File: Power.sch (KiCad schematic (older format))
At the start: 46 parts, among them J7 AUX, J8 MCU_CURRENT, J9 RAM_CURRENT, Q2 IRLML6402, U1 ATXMEGA128A1U-AU, U2 SN74AHC573PW, U4 LM3671MF

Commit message: Finished?
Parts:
- removed C33, C?: 100n, IPC7351-Nominal:CAPC1005X55, symbol C-0402
- removed D?: SS12, IPC7351-Nominal:DIOM5326X292, symbol SS12
- removed Q2, Q?: IRLML6402, smd-semi:SOT-23, symbol IRLML6402
- removed Q?: MMUN2231L, smd-semi:SOT-23, symbol MMUN2231L
- removed Q?: MMUN2111L, smd-semi:SOT-23, symbol MMUN2111L
- removed R13: 100k, IPC7351-Nominal:RESCAXE80P160X320X70-8, symbol RESPACK-4X0603-CONV
- removed R? (x4): 3k3, IPC7351-Nominal:RESCAXE80P160X320X70-8, symbol RESPACK-4X0603-CONV
- added J10: POWER, conn-fci:CONN-10118194-0001LF-FCI, symbol CONN-10118194-0001LF-UUSB-B
- added R13, R16: 365, IPC7351-Nominal:RESC1005X40, symbol R-0402
- added R17: 3k3, IPC7351-Nominal:RESCAXE80P160X320X70-8, symbol RESPACK-4X0603-CONV
- added TP1: GND, manuf:TESTPOINT-KEYSTONE-5018, symbol TESTPOINT
- added U7: TPS2110A, IPC7351-Nominal:SOP65P640X110-8, symbol TPS2110A
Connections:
- net FILT_VBUS: now also U7.6 (IN2); no longer C32.1
- net GND: now also C32.1, J10.5 (GND), J10.SH (SHIELD), R13.2, R17.4, TP1.1, U7.2 (D1), U7.5 (GND)
- net VBUS: now also U7.7 (OUT)
- net ALT_VBUS: now reaches C32.2
- net ALT_VBUS: now also J10.1 (V+), R16.1, U7.8 (IN1)
- new net: R16.2, R17.1
- new net: R17.7, R17.8
- new net: R17.2, R17.3
- new net: R17.5, R17.6, U7.3 (VSNS)
- new net: R13.1, U7.4 (ILIM)
- no-connect marks 0 -> 4
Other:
- note added: "I_lim = 250V/R_lim = 685mA\nTypical inrush 250mA\nout = (in1 ≥ 3.38V ? in1 : max(in1, in2))"
- moved on the sheet: C13, C20, C21, C34, C35, E1, L2, U4

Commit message: Reannotate
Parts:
- renumbered C32 to C12, C35 to C13, C24 to C14, C25 to C15, C26 to C16, C3 to C17, C6 to C18, C5 to C19, C4 to C20, C8 to C21, C7 to C22, C28 to C23, C10 to C24, C9 to C25, C34 to C26, C12 to C27, C11 to C28, C13 to C29, C27 to C30, C1 to C31, C2 to C32, C20 to C33, C21 to C34, J7 to J10, J10 to J7, L2 to L1, R14 to R18, R15 to R19, R16 to R20, R17 to R21, R13 to R22, TP1 to TP5, U2 to U4, U7 to U6, U4 to U7

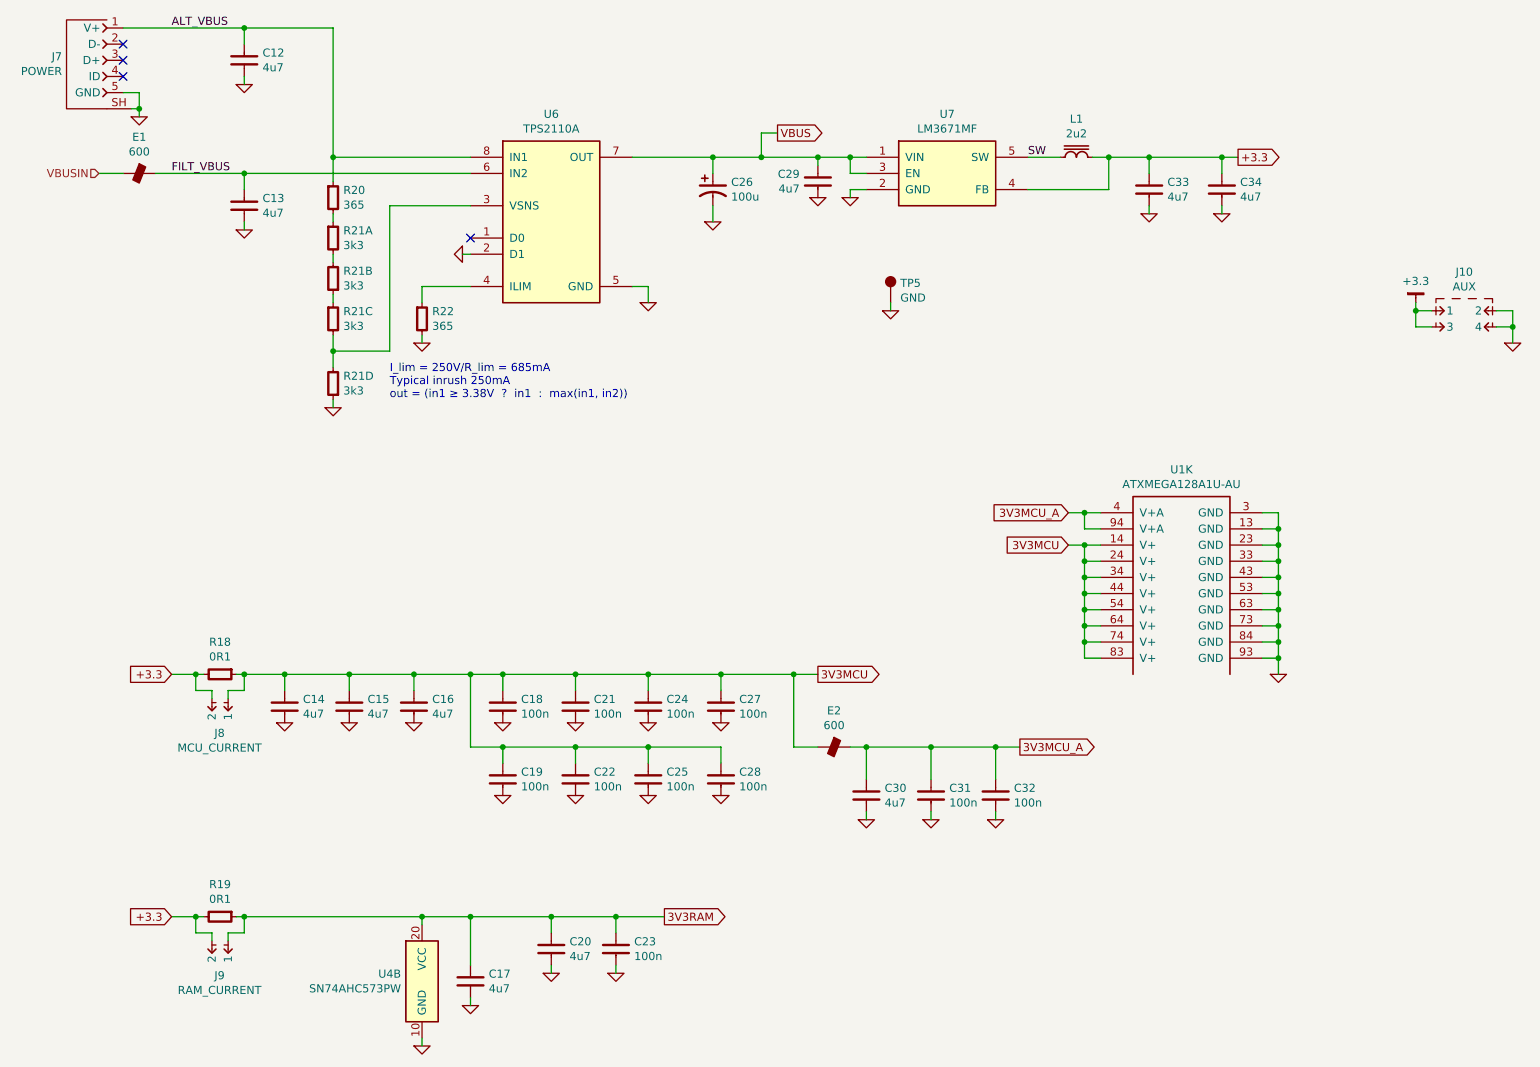
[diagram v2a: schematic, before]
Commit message: Schematic tidy-ups and add VBUS sense
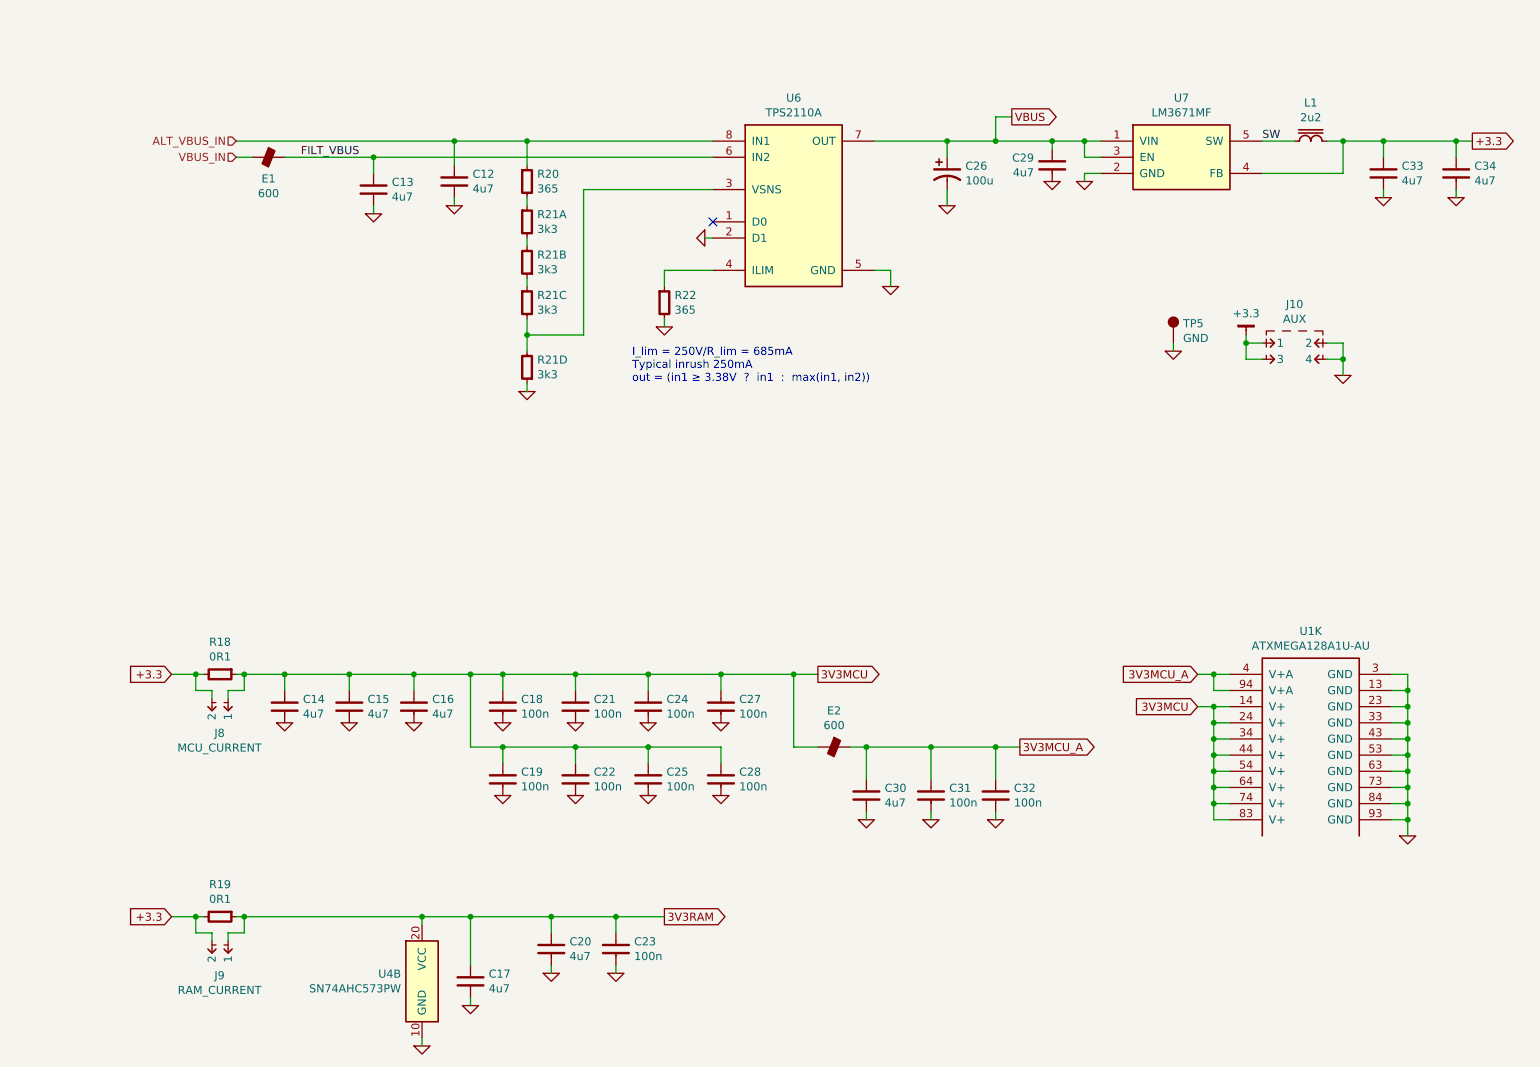
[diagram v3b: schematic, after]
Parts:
- removed J7: POWER, conn-fci:CONN-10118194-0001LF-FCI, symbol CONN-10118194-0001LF-UUSB-B
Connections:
- net ALT_VBUS renamed ALT_VBUS_IN
- net VBUSIN renamed VBUS_IN
- no-connect marks 4 -> 1
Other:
- moved on the sheet: C12, C13, C26, C29, C33, C34, E1, J10, L1, R20, R21A, R21B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

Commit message: Rearrange Power schematic a bit
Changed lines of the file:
@@
 Connection ~ 9100 5600
 Wire Wire Line
-	9100 4700 9100 4800
-Wire Wire Line
-	9100 4800 9100 4900
-Wire Wire Line
-	9100 4900 9100 5000
-Wire Wire Line
-	9100 5000 9100 5100
-Wire Wire Line
-	9100 5100 9100 5200
-Wire Wire Line
-	9100 5200 9100 5300
-Wire Wire Line
-	9100 5300 9100 5400
-Wire Wire Line
-	9100 5400 9100 5500
-Wire Wire Line
-	9100 5500 9100 5600
-Wire Wire Line
-	9100 5600 9100 5700
+	9100 4700 9100 5700
 Wire Wire Line
 	3000 6200 3000 6250
@@
 	3000 7000 3000 6950
 Wire Wire Line
-	5650 5150 5750 5150
-Wire Wire Line
-	5750 5150 6150 5150
-Wire Wire Line
-	6150 5150 6550 5150
-Wire Wire Line
-	6550 5150 6700 5150
+	5650 5150 6700 5150
 Wire Wire Line
 	6150 5150 6150 5350
@@
 	5750 5600 5750 5550
 Wire Wire Line
-	1850 4700 1900 4700
-Wire Wire Line
-	1900 4700 2150 4700
-Wire Wire Line
-	2150 4700 2550 4700
-Wire Wire Line
-	2550 4700 2950 4700
-Wire Wire Line
-	2950 4700 3300 4700
-Wire Wire Line
-	3300 4700 3500 4700
-Wire Wire Line
-	3500 4700 3950 4700
-Wire Wire Line
-	3950 4700 4400 4700
-Wire Wire Line
-	4400 4700 4850 4700
-Wire Wire Line
-	4850 4700 5300 4700
-Wire Wire Line
-	5300 4700 5450 4700
+	1850 4700 5450 4700
 Wire Wire Line
 	2150 4700 2150 4800
@@
 	5450 5150 5300 5150
 Wire Wire Line
-	1450 4700 1600 4700
-Wire Wire Line
-	1600 4700 1650 4700
+	1450 4700 1650 4700
 Connection ~ 2150 4700
 Wire Wire Line
@@
 	8200 2650 8100 2650
 Wire Wire Line
-	8100 2600 8100 2650
-Wire Wire Line
-	8100 2650 8100 2750
+	8100 2600 8100 2750
 Wire Wire Line
 	8100 2750 8200 2750
@@
 	9400 1400 9400 1500
 Wire Wire Line
-	8600 1400 8700 1400
-Wire Wire Line
-	8700 1400 8950 1400
-Wire Wire Line
-	8950 1400 9400 1400
-Wire Wire Line
-	9400 1400 9500 1400
-Wire Wire Line
-	8700 2650 8700 2750
-Wire Wire Line
-	8700 2750 8700 2850
+	8600 1400 9500 1400
+Wire Wire Line
+	8700 2650 8700 2850
 Wire Wire Line
 	8700 2650 8600 2650
@@
 	6650 1250 6550 1250
 Wire Wire Line
-	6550 1250 6550 1400
+	6550 1400 6550 1250
 Connection ~ 6550 1400
 Connection ~ 4850 4700
@@
 	3300 4700 3300 5150
 Wire Wire Line
-	3300 5150 3500 5150
-Wire Wire Line
-	3500 5150 3950 5150
-Wire Wire Line
-	3950 5150 4400 5150
-Wire Wire Line
-	4400 5150 4850 5150
+	3300 5150 4850 5150
 Wire Wire Line
 	4850 5150 4850 5250
@@
 Connection ~ 5300 4700
 Wire Wire Line
-	7800 4700 7900 4700
-Wire Wire Line
-	7900 4700 8000 4700
+	7800 4700 8000 4700
 Wire Wire Line
 	7900 4700 7900 4800
@@
 Connection ~ 7900 4700
 Wire Wire Line
-	7800 4900 7900 4900
-Wire Wire Line
-	7900 4900 8000 4900
+	7800 4900 8000 4900
 Wire Wire Line
 	7900 5000 8000 5000
@@
 Connection ~ 7900 5500
 Wire Wire Line
-	7900 4900 7900 5000
-Wire Wire Line
-	7900 5000 7900 5100
-Wire Wire Line
-	7900 5100 7900 5200
-Wire Wire Line
-	7900 5200 7900 5300
-Wire Wire Line
-	7900 5300 7900 5400
-Wire Wire Line
-	7900 5400 7900 5500
-Wire Wire Line
-	7900 5500 7900 5600
+	7900 4900 7900 5600
 Wire Wire Line
 	3800 6200 3800 6300
@@
 	4200 6550 4200 6500
 Wire Wire Line
-	1850 6200 1900 6200
-Wire Wire Line
-	1900 6200 3000 6200
-Wire Wire Line
-	3000 6200 3300 6200
-Wire Wire Line
-	3300 6200 3800 6200
-Wire Wire Line
-	3800 6200 4200 6200
-Wire Wire Line
-	4200 6200 4500 6200
-Wire Wire Line
-	1450 6200 1600 6200
-Wire Wire Line
-	1600 6200 1650 6200
+	1850 6200 4500 6200
+Wire Wire Line
+	1450 6200 1650 6200
 Wire Wire Line
 	1700 6350 1700 6300
@@
 Connection ~ 3000 6200
 Wire Wire Line
-	5800 1400 6250 1400
-Wire Wire Line
-	6250 1400 6550 1400
-Wire Wire Line
-	6550 1400 6900 1400
-Wire Wire Line
-	6900 1400 7100 1400
-Wire Wire Line
-	7100 1400 7200 1400
-Wire Wire Line
-	1850 1400 3200 1400
-Wire Wire Line
-	3200 1400 3650 1400
+	5800 1400 7200 1400
+Wire Wire Line
+	1850 1400 4800 1400
 Wire Wire Line
 	4750 2000 4800 2000
@@
 	4500 2550 4500 2500
 Wire Wire Line
-	2150 1500 2700 1500
-Wire Wire Line
-	2700 1500 4800 1500
-Wire Wire Line
-	3650 1400 3650 1400
+	2150 1500 4800 1500
 Wire Wire Line
 	3650 1400 3650 1550
-Wire Wire Line
-	3650 1400 4800 1400
 Wire Wire Line
 	3650 2950 3650 2900
@@
 	3650 2050 3650 2000
 Wire Wire Line
-	3650 2500 3650 2600
-Wire Wire Line
-	3650 2600 3650 2700
+	3650 2500 3650 2700
 Wire Wire Line
 	4000 1700 4000 2600

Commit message: Decrease LED current
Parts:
- R21: value 3k3 -> 15k; BOM DIST DIGIKEY YC164J-3.3KCT-ND -> DIST DIGIKEY YC164J-15KCT-ND
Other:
- note added: "I_lim = 250V/R_lim = 685mA\nTypical inrush 250mA\nout = (in1 ≥ 3.2V ? in1 : max(in1, in2))"
- note removed: "I_lim = 250V/R_lim = 685mA\nTypical inrush 250mA\nout = (in1 ≥ 3.38V ? in1 : max(in1, in2))"
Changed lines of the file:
@@
 $EndComp
 Text Notes 4300 2900 0    50   ~ 0
-I_lim = 250V/R_lim = 685mA\nTypical inrush 250mA\nout = (in1 ≥ 3.38V  ?  in1  :  max(in1, in2))
+I_lim = 250V/R_lim = 685mA\nTypical inrush 250mA\nout = (in1 ≥ 3.2V  ?  in1  :  max(in1, in2))
 $Comp
 L RESPACK-4X0603-CONV R?
@@
 AR Path="/56EF633C/56F0A0E0" Ref="R21"  Part="1"
 F 0 "R21" H 3713 1946 50  0000 L CNN
-F 1 "3k3" H 3713 1855 50  0000 L CNN
+F 1 "15k" H 3713 1855 50  0000 L CNN
 F 2 "IPC7351-Nominal:RESCAXE80P160X320X70-8" H 3650 1900 50  0001 C CNN
 F 3 "" H 3650 1950 60  0000 C CNN
-F 4 "DIST DIGIKEY YC164J-3.3KCT-ND" H 3650 1900 60  0001 C CNN "BOM"
+F 4 "DIST DIGIKEY YC164J-15KCT-ND" H 3650 1900 60  0001 C CNN "BOM"
 	1    3650 1900
 	1    0    0    -1
@@
 AR Path="/56EF633C/56F0A2D7" Ref="R21"  Part="2"
 F 0 "R21" H 3587 2104 50  0000 R CNN
-F 1 "3k3" H 3587 2195 50  0000 R CNN
+F 1 "15k" H 3587 2195 50  0000 R CNN
 F 2 "IPC7351-Nominal:RESCAXE80P160X320X70-8" H 3650 2150 50  0001 C CNN
 F 3 "" H 3650 2200 60  0000 C CNN
-F 4 "DIST DIGIKEY YC164J-3.3KCT-ND" H 3650 2150 60  0001 C CNN "BOM"
+F 4 "DIST DIGIKEY YC164J-15KCT-ND" H 3650 2150 60  0001 C CNN "BOM"
 	2    3650 2150
 	-1   0    0    1
@@
 AR Path="/56EF633C/56F0A367" Ref="R21"  Part="3"
 F 0 "R21" H 3713 2446 50  0000 L CNN
-F 1 "3k3" H 3713 2355 50  0000 L CNN
+F 1 "15k" H 3713 2355 50  0000 L CNN
 F 2 "IPC7351-Nominal:RESCAXE80P160X320X70-8" H 3650 2400 50  0001 C CNN
 F 3 "" H 3650 2450 60  0000 C CNN
-F 4 "DIST DIGIKEY YC164J-3.3KCT-ND" H 3650 2400 60  0001 C CNN "BOM"
+F 4 "DIST DIGIKEY YC164J-15KCT-ND" H 3650 2400 60  0001 C CNN "BOM"
 	3    3650 2400
 	1    0    0    -1
@@
 AR Path="/56EF633C/56F0A408" Ref="R21"  Part="4"
 F 0 "R21" H 3587 2754 50  0000 R CNN
-F 1 "3k3" H 3587 2845 50  0000 R CNN
+F 1 "15k" H 3587 2845 50  0000 R CNN
 F 2 "IPC7351-Nominal:RESCAXE80P160X320X70-8" H 3650 2800 50  0001 C CNN
 F 3 "" H 3650 2850 60  0000 C CNN
-F 4 "DIST DIGIKEY YC164J-3.3KCT-ND" H 3650 2800 60  0001 C CNN "BOM"
+F 4 "DIST DIGIKEY YC164J-15KCT-ND" H 3650 2800 60  0001 C CNN "BOM"
 	4    3650 2800
 	-1   0    0    1
